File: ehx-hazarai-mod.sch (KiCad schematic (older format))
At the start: 31 parts, among them P1 in filt, P2 fsw +, P3 loop in, P4 beat in, P5 beat out, P6 loop out, P7 5v in, P8 in nofilt, P9 fsw gnd, Q1 BC547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

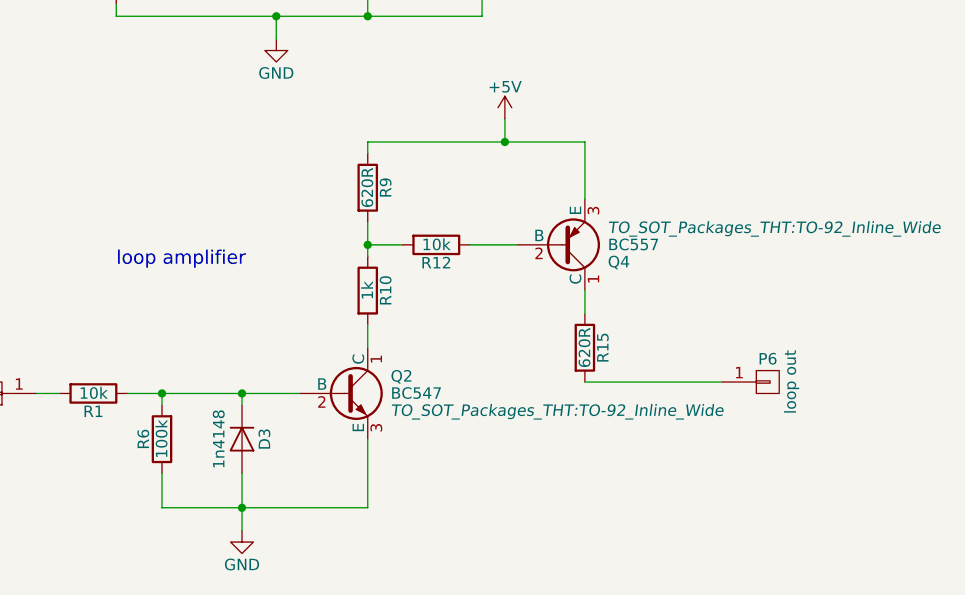
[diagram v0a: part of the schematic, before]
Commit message: updated connections and i/o.. should work now..
needs a little more layout
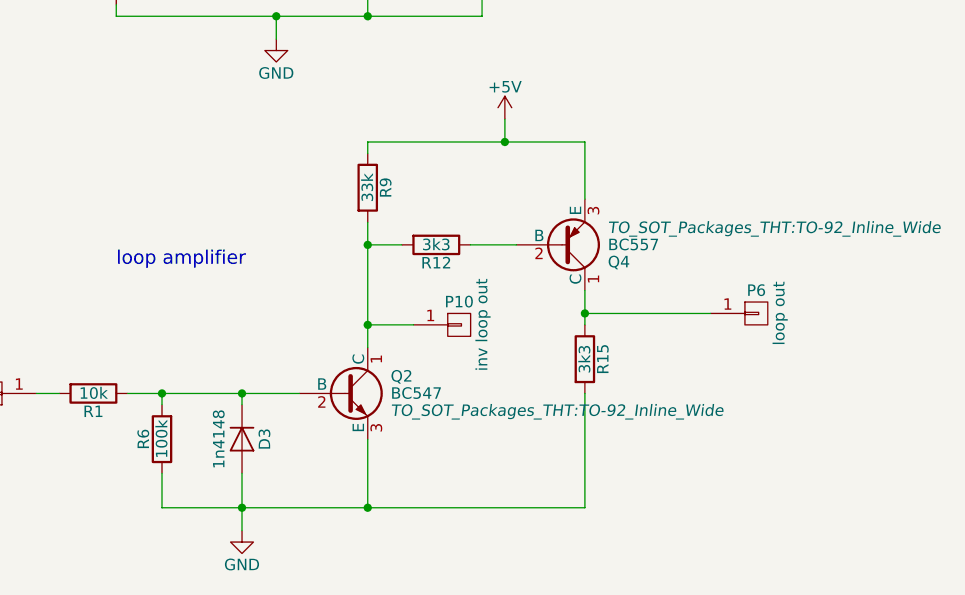
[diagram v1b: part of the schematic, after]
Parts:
- removed R10: 1k, Resistors_ThroughHole:Resistor_Vertical_RM5mm, symbol R
- added P10: inv loop out, Pin_Headers:Pin_Header_Straight_1x01_Pitch2.54mm, symbol CONN_01X01
- P1, P2, P3, P4, P5, P6, P7, P8, P9: footprint Pin_Headers:Pin_Header_Straight_1x01 -> Pin_Headers:Pin_Header_Straight_1x01_Pitch2.54mm
- R12: value 10k -> 3k3
- R15: value 620R -> 3k3
- R9: value 620R -> 33k
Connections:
- net GND: now also R15.2
- net at Q2.1 (C): now also R12.2, R9.2, P10.1 (P1)
- net at Q4.1 (C), R15.1: now also P6.1 (P1)
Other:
- moved on the sheet: P6, R15
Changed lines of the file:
@@
 F 0 "P4" H 1250 4600 50  0000 C CNN
 F 1 "beat in" V 1350 4500 50  0000 C CNN
-F 2 "Pin_Headers:Pin_Header_Straight_1x01" H 1250 4500 50  0001 C CNN
+F 2 "Pin_Headers:Pin_Header_Straight_1x01_Pitch2.54mm" H 1250 4500 50  0001 C CNN
 F 3 "" H 1250 4500 50  0000 C CNN
 	1    1250 4500
@@
 F 0 "P3" H 1200 6650 50  0000 C CNN
 F 1 "loop in" V 1300 6550 50  0000 C CNN
-F 2 "Pin_Headers:Pin_Header_Straight_1x01" H 1200 6550 50  0001 C CNN
+F 2 "Pin_Headers:Pin_Header_Straight_1x01_Pitch2.54mm" H 1200 6550 50  0001 C CNN
 F 3 "" H 1200 6550 50  0000 C CNN
 	1    1200 6550
@@
 	1    0    0    -1
 $EndComp
-Wire Wire Line
-	2250 2550 2900 2550
-Wire Wire Line
-	2300 2300 2300 2600
-Wire Wire Line
-	2300 2900 2300 2950
-Wire Wire Line
-	1800 2950 4400 2950
-Wire Wire Line
-	1800 2950 1800 2900
-Wire Wire Line
-	2650 2950 2650 2900
-Connection ~ 2300 2950
-Wire Wire Line
-	2650 2550 2650 2600
-Connection ~ 2300 2550
-Connection ~ 2650 2550
-Wire Wire Line
-	3200 2550 3300 2550
-Wire Wire Line
-	3600 2950 3600 2750
-Connection ~ 2650 2950
-Wire Wire Line
-	1650 2300 2300 2300
-Wire Wire Line
-	3600 2350 4350 2350
-Connection ~ 3600 2950
-Wire Wire Line
-	1800 2550 1800 2600
-Connection ~ 1800 2550
-Wire Wire Line
-	1450 4500 1900 4500
-Wire Wire Line
-	1750 4500 1750 4550
-Connection ~ 1750 4500
-Wire Wire Line
-	2200 4500 2350 4500
-Wire Wire Line
-	2650 4500 3050 4500
-Connection ~ 2850 4500
-Wire Wire Line
-	2850 4900 2850 4800
-Wire Wire Line
-	1750 4900 3350 4900
-Wire Wire Line
-	1750 4900 1750 4850
-Wire Wire Line
-	3350 4900 3350 4700
-Connection ~ 2850 4900
-Wire Wire Line
-	3350 4150 3350 4300
-Wire Wire Line
-	3800 4250 3350 4250
-Connection ~ 3350 4250
-Wire Wire Line
-	3350 3400 3350 3850
 $Comp
 L +5V #PWR02
@@
 F 0 "P5" H 4600 4350 50  0000 C CNN
 F 1 "beat out" V 4700 4250 50  0000 C CNN
-F 2 "Pin_Headers:Pin_Header_Straight_1x01" H 4600 4250 50  0001 C CNN
+F 2 "Pin_Headers:Pin_Header_Straight_1x01_Pitch2.54mm" H 4600 4250 50  0001 C CNN
 F 3 "" H 4600 4250 50  0000 C CNN
 	1    4600 4250
 	1    0    0    -1
 $EndComp
-Wire Wire Line
-	4100 4250 4400 4250
 $Comp
 L GND #PWR03
@@
 $EndComp
 $Comp
-L R R10
-U 1 1 57FAEF69
-P 2850 6100
-F 0 "R10" V 2930 6100 50  0000 C CNN
-F 1 "1k" V 2850 6100 50  0000 C CNN
-F 2 "Resistors_ThroughHole:Resistor_Vertical_RM5mm" V 2780 6100 50  0001 C CNN
-F 3 "" H 2850 6100 50  0000 C CNN
-	1    2850 6100
-	1    0    0    -1
-$EndComp
-$Comp
 L R R9
 U 1 1 57FAEFAE
 P 2850 5650
 F 0 "R9" V 2930 5650 50  0000 C CNN
-F 1 "620R" V 2850 5650 50  0000 C CNN
+F 1 "33k" V 2850 5650 50  0000 C CNN
 F 2 "Resistors_ThroughHole:Resistor_Vertical_RM5mm" V 2780 5650 50  0001 C CNN
 F 3 "" H 2850 5650 50  0000 C CNN
@@
 P 3150 5900
 F 0 "R12" V 3230 5900 50  0000 C CNN
-F 1 "10k" V 3150 5900 50  0000 C CNN
+F 1 "3k3" V 3150 5900 50  0000 C CNN
 F 2 "Resistors_ThroughHole:Resistor_Vertical_RM5mm" V 3080 5900 50  0001 C CNN
 F 3 "" H 3150 5900 50  0000 C CNN
@@
 L R R15
 U 1 1 57FAF16A
-P 3800 6350
-F 0 "R15" V 3880 6350 50  0000 C CNN
-F 1 "620R" V 3800 6350 50  0000 C CNN
-F 2 "Resistors_ThroughHole:Resistor_Vertical_RM5mm" V 3730 6350 50  0001 C CNN
-F 3 "" H 3800 6350 50  0000 C CNN
-	1    3800 6350
+P 3800 6400
+F 0 "R15" V 3880 6400 50  0000 C CNN
+F 1 "3k3" V 3800 6400 50  0000 C CNN
+F 2 "Resistors_ThroughHole:Resistor_Vertical_RM5mm" V 3730 6400 50  0001 C CNN
+F 3 "" H 3800 6400 50  0000 C CNN
+	1    3800 6400
 	1    0    0    -1
 $EndComp
@@
 	1    0    0    -1
 $EndComp
-Wire Wire Line
-	1400 6550 1500 6550
-Wire Wire Line
-	1800 6550 2550 6550
-Wire Wire Line
-	2300 6550 2300 6600
-Connection ~ 2300 6550
-Wire Wire Line
-	1950 6550 1950 6600
-Connection ~ 1950 6550
-Wire Wire Line
-	2850 6350 2850 6250
-Wire Wire Line
-	2850 5800 2850 5950
-Wire Wire Line
-	3000 5900 2850 5900
-Connection ~ 2850 5900
-Wire Wire Line
-	3300 5900 3500 5900
-Wire Wire Line
-	3800 5450 3800 5700
-Wire Wire Line
-	3800 6100 3800 6200
-Wire Wire Line
-	3800 6500 4400 6500
-Wire Wire Line
-	2850 7050 2850 6750
-Wire Wire Line
-	1950 7050 2850 7050
-Wire Wire Line
-	2300 6900 2300 7150
-Wire Wire Line
-	1950 6900 1950 7050
-Connection ~ 2300 7050
-Wire Wire Line
-	2850 5450 3800 5450
-Wire Wire Line
-	2850 5450 2850 5500
-Wire Wire Line
-	3450 5350 3450 5450
-Connection ~ 3450 5450
 $Comp
 L CONN_01X01 P6
 U 1 1 57FB036C
-P 4600 6500
-F 0 "P6" H 4600 6600 50  0000 C CNN
-F 1 "loop out" V 4700 6500 50  0000 C CNN
-F 2 "Pin_Headers:Pin_Header_Straight_1x01" H 4600 6500 50  0001 C CNN
-F 3 "" H 4600 6500 50  0000 C CNN
-	1    4600 6500
+P 4550 6200
+F 0 "P6" H 4550 6300 50  0000 C CNN
+F 1 "loop out" V 4650 6200 50  0000 C CNN
+F 2 "Pin_Headers:Pin_Header_Straight_1x01_Pitch2.54mm" H 4550 6200 50  0001 C CNN
+F 3 "" H 4550 6200 50  0000 C CNN
+	1    4550 6200
 	1    0    0    -1
 $EndComp
@@
 F 0 "P7" H 1250 3650 50  0000 C CNN
 F 1 "5v in" V 1350 3550 50  0000 C CNN
-F 2 "Pin_Headers:Pin_Header_Straight_1x01" H 1250 3550 50  0001 C CNN
+F 2 "Pin_Headers:Pin_Header_Straight_1x01_Pitch2.54mm" H 1250 3550 50  0001 C CNN
 F 3 "" H 1250 3550 50  0000 C CNN
 	1    1250 3550
@@
 	1    0    0    -1
 $EndComp
-Wire Wire Line
-	1700 3550 1700 3500
-Connection ~ 1700 3550
-Wire Wire Line
-	1450 3550 1700 3550
 Text Label 2750 2950 0    60   ~ 0
 GND
@@
 F 0 "P8" H 1450 2400 50  0000 C CNN
 F 1 "in nofilt" V 1550 2300 50  0000 C CNN
-F 2 "Pin_Headers:Pin_Header_Straight_1x01" H 1450 2300 50  0001 C CNN
+F 2 "Pin_Headers:Pin_Header_Straight_1x01_Pitch2.54mm" H 1450 2300 50  0001 C CNN
 F 3 "" H 1450 2300 50  0000 C CNN
 	1    1450 2300
@@
 F 0 "P1" H 1200 2650 50  0000 C CNN
 F 1 "in filt" V 1300 2550 50  0000 C CNN
-F 2 "Pin_Headers:Pin_Header_Straight_1x01" H 1200 2550 50  0001 C CNN
+F 2 "Pin_Headers:Pin_Header_Straight_1x01_Pitch2.54mm" H 1200 2550 50  0001 C CNN
 F 3 "" H 1200 2550 50  0000 C CNN
 	1    1200 2550
 	-1   0    0    -1
 $EndComp
-Wire Wire Line
-	1400 2550 1950 2550
 $Comp
 L CONN_01X01 P9
@@
 F 0 "P9" H 4600 3050 50  0000 C CNN
 F 1 "fsw gnd" V 4700 2950 50  0000 C CNN
-F 2 "Pin_Headers:Pin_Header_Straight_1x01" H 4600 2950 50  0001 C CNN
+F 2 "Pin_Headers:Pin_Header_Straight_1x01_Pitch2.54mm" H 4600 2950 50  0001 C CNN
 F 3 "" H 4600 2950 50  0000 C CNN
 	1    4600 2950
@@
 F 0 "P2" H 4550 2450 50  0000 C CNN
 F 1 "fsw +" V 4650 2350 50  0000 C CNN
-F 2 "Pin_Headers:Pin_Header_Straight_1x01" H 4550 2350 50  0001 C CNN
+F 2 "Pin_Headers:Pin_Header_Straight_1x01_Pitch2.54mm" H 4550 2350 50  0001 C CNN
 F 3 "" H 4550 2350 50  0000 C CNN
 	1    4550 2350
@@
 $EndComp
 Wire Wire Line
+	2250 2550 2900 2550
+Wire Wire Line
+	2300 2300 2300 2600
+Wire Wire Line
+	2300 2900 2300 2950
+Wire Wire Line
+	1800 2950 4400 2950
+Wire Wire Line
+	1800 2950 1800 2900
+Wire Wire Line
+	2650 2950 2650 2900
+Connection ~ 2300 2950
+Wire Wire Line
+	2650 2550 2650 2600
+Connection ~ 2300 2550
+Connection ~ 2650 2550
+Wire Wire Line
+	3200 2550 3300 2550
+Wire Wire Line
+	3600 2950 3600 2750
+Connection ~ 2650 2950
+Wire Wire Line
+	1650 2300 2300 2300
+Wire Wire Line
+	3600 2350 4350 2350
+Connection ~ 3600 2950
+Wire Wire Line
+	1800 2550 1800 2600
+Connection ~ 1800 2550
+Wire Wire Line
+	1450 4500 1900 4500
+Wire Wire Line
+	1750 4500 1750 4550
+Connection ~ 1750 4500
+Wire Wire Line
+	2200 4500 2350 4500
+Wire Wire Line
+	2650 4500 3050 4500
+Connection ~ 2850 4500
+Wire Wire Line
+	2850 4900 2850 4800
+Wire Wire Line
+	1750 4900 3350 4900
+Wire Wire Line
+	1750 4900 1750 4850
+Wire Wire Line
+	3350 4900 3350 4700
+Connection ~ 2850 4900
+Wire Wire Line
+	3350 4150 3350 4300
+Wire Wire Line
+	3800 4250 3350 4250
+Connection ~ 3350 4250
+Wire Wire Line
+	3350 3400 3350 3850
+Wire Wire Line
+	4100 4250 4400 4250
+Wire Wire Line
+	1400 6550 1500 6550
+Wire Wire Line
+	1800 6550 2550 6550
+Wire Wire Line
+	2300 6550 2300 6600
+Connection ~ 2300 6550
+Wire Wire Line
+	1950 6550 1950 6600
+Connection ~ 1950 6550
+Wire Wire Line
+	2850 5800 2850 6350
+Wire Wire Line
+	3000 5900 2850 5900
+Connection ~ 2850 5900
+Wire Wire Line
+	3300 5900 3500 5900
+Wire Wire Line
+	3800 5450 3800 5700
+Wire Wire Line
+	3800 6100 3800 6250
+Wire Wire Line
+	2850 7050 2850 6750
+Wire Wire Line
+	1950 7050 3800 7050
+Wire Wire Line
+	2300 6900 2300 7150
+Wire Wire Line
+	1950 6900 1950 7050
+Connection ~ 2300 7050
+Wire Wire Line
+	2850 5450 3800 5450
+Wire Wire Line
+	2850 5450 2850 5500
+Wire Wire Line
+	3450 5350 3450 5450
+Connection ~ 3450 5450
+Wire Wire Line
+	1700 3550 1700 3500
+Connection ~ 1700 3550
+Wire Wire Line
+	1450 3550 1700 3550
+Wire Wire Line
+	1400 2550 1950 2550
+Wire Wire Line
 	4200 2900 4200 2950
 Connection ~ 4200 2950
@@
 	2450 2950 2450 3150
 Connection ~ 2450 2950
+Wire Wire Line
+	4350 6200 3800 6200
+Connection ~ 3800 6200
+Wire Wire Line
+	3800 7050 3800 6550
+Connection ~ 2850 7050
+$Comp
+L CONN_01X01 P10
+U 1 1 58E01D1C
+P 3250 6250
+F 0 "P10" H 3250 6350 50  0000 C CNN
+F 1 "inv loop out" V 3350 6250 50  0000 C CNN
+F 2 "Pin_Headers:Pin_Header_Straight_1x01_Pitch2.54mm" H 3250 6250 50  0001 C CNN
+F 3 "" H 3250 6250 50  0000 C CNN
+	1    3250 6250
+	1    0    0    -1
+$EndComp
+Wire Wire Line
+	3050 6250 2850 6250
+Connection ~ 2850 6250
 $EndSCHEMATC
